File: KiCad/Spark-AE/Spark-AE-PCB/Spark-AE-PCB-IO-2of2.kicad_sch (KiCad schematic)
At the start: 16 parts, among them U6 Connector_Micro_SD_Card_Yamai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, U7 MCP6002-xSN, U8 74LVC1G125

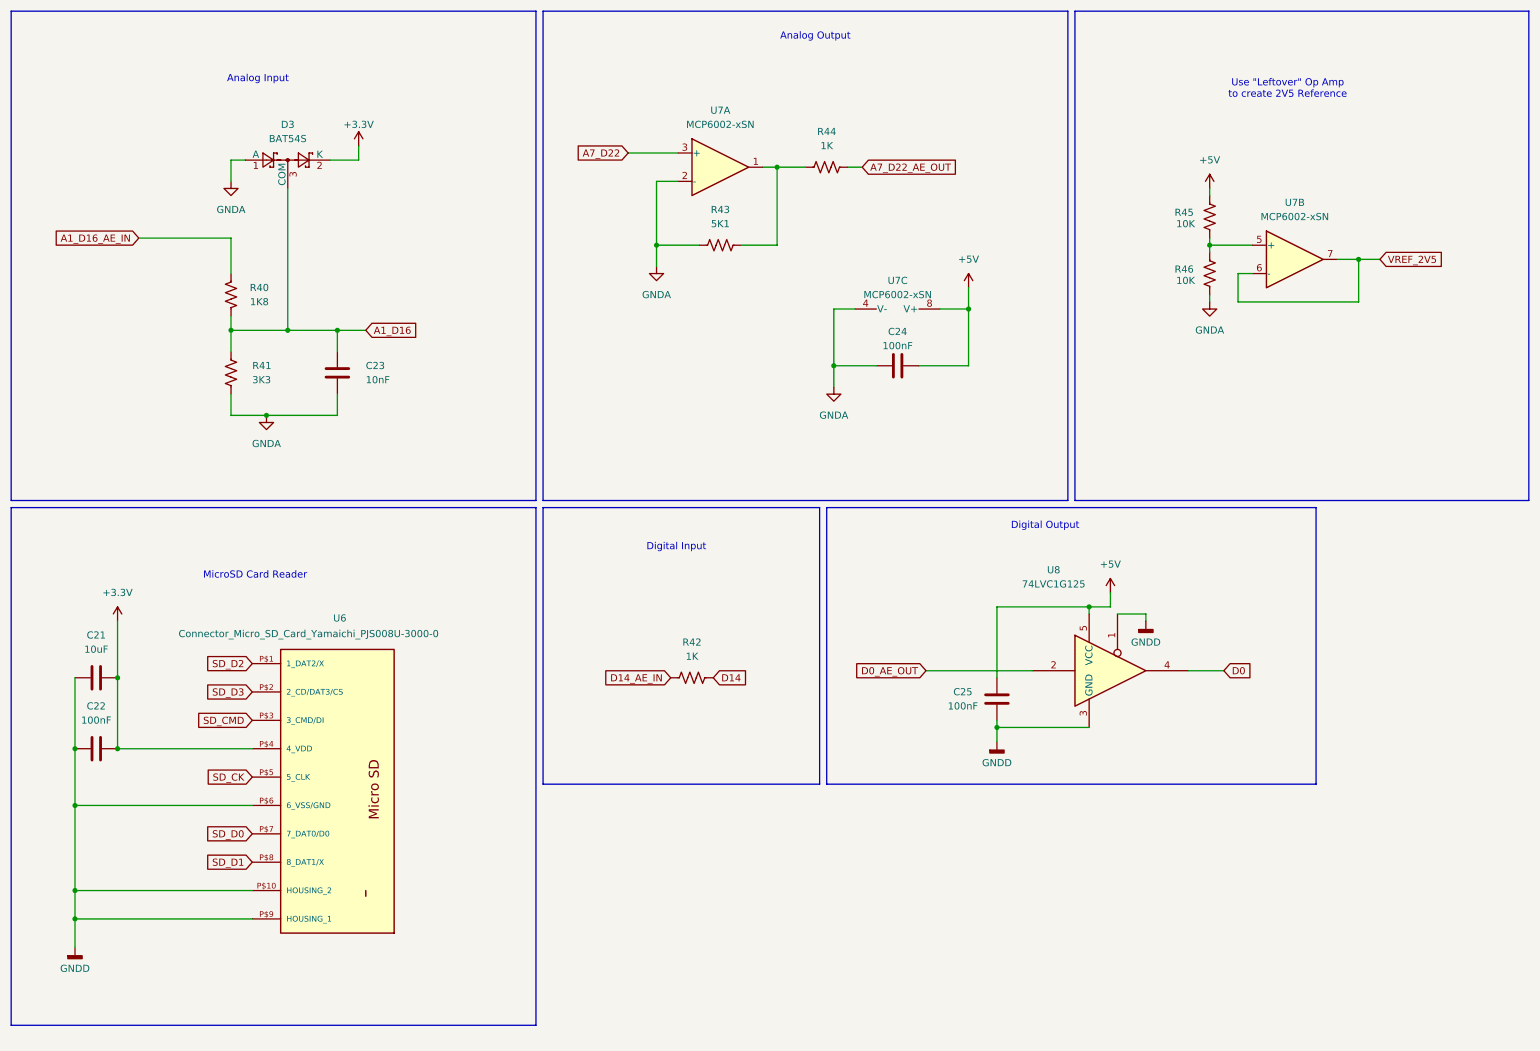
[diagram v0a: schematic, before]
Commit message: assigned footprints & sorted ratsnest
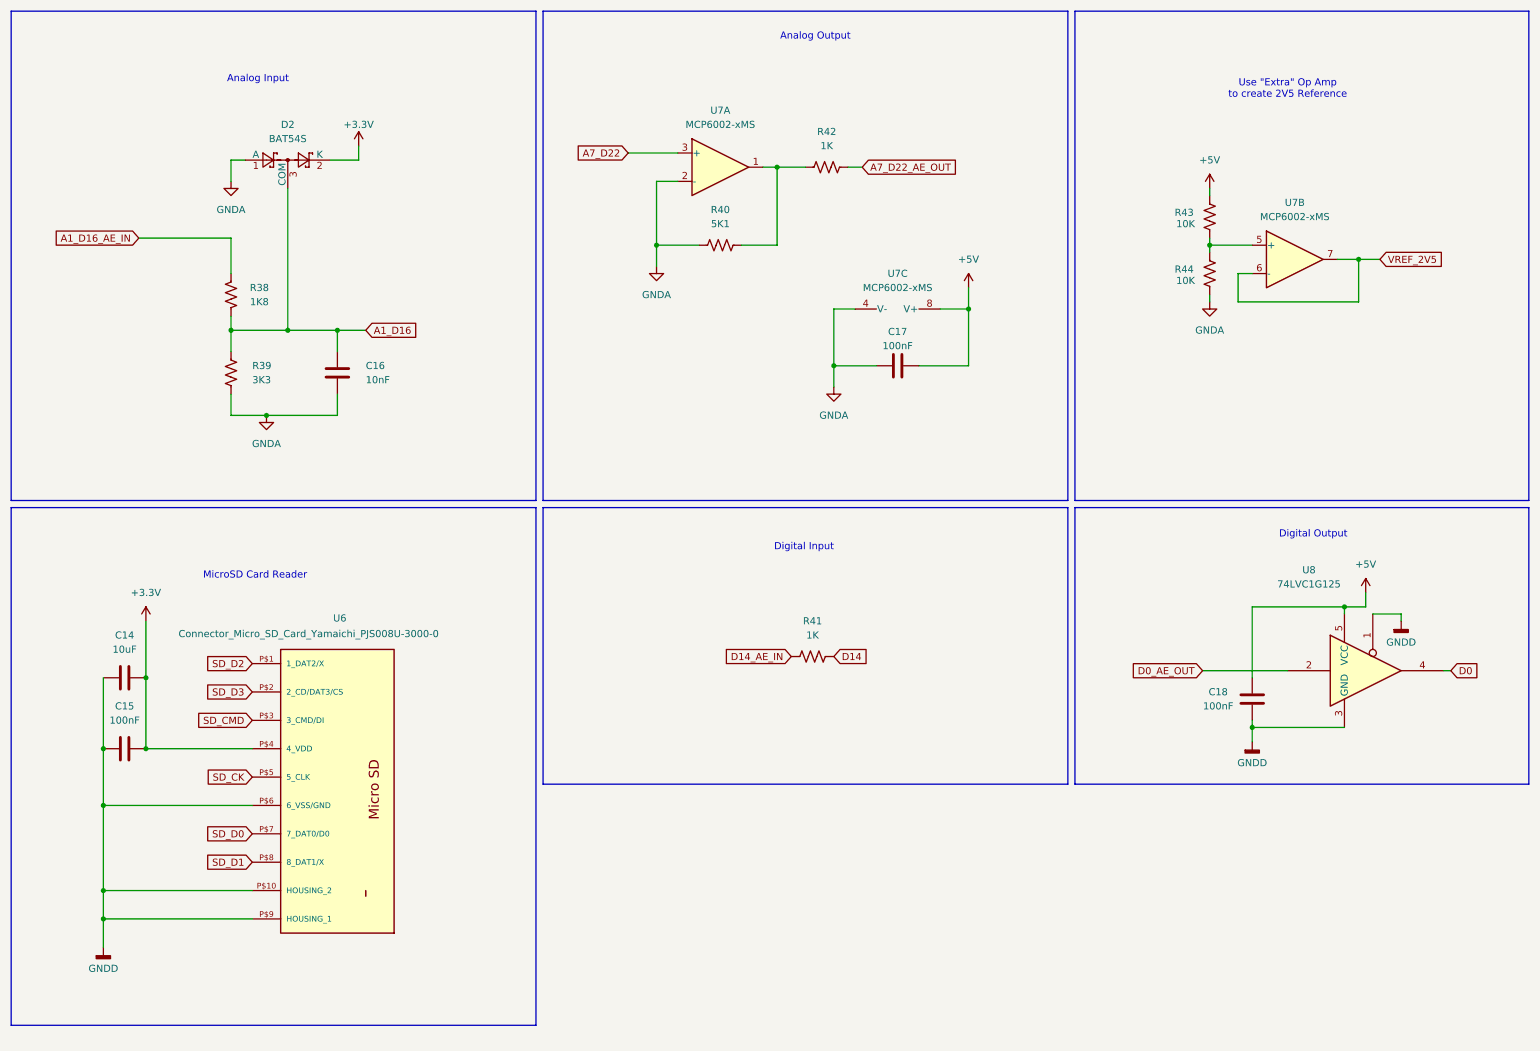
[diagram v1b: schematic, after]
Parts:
- removed U7: MCP6002-xSN, symbol Amplifier_Operational:MCP6002-xSN
- added U7: MCP6002-xMS, clectric-diy:Amplifier_Operational_Microchip_MCP6002T-I_MS, symbol Amplifier_Operational:MCP6002-xMS
- C14: renamed from C21; footprint (none) -> Capacitor_SMD:C_0805_2012Metric
- C15: renamed from C22; footprint (none) -> Capacitor_SMD:C_0603_1608Metric
- C16: renamed from C23; footprint (none) -> Capacitor_SMD:C_0603_1608Metric
- C17: renamed from C24; footprint (none) -> Capacitor_SMD:C_0603_1608Metric
- C18: renamed from C25; footprint (none) -> Capacitor_SMD:C_0603_1608Metric
- R38: renamed from R40; footprint (none) -> Resistor_SMD:R_0603_1608Metric
- R39: renamed from R41; footprint (none) -> Resistor_SMD:R_0603_1608Metric
- R40: renamed from R43; footprint (none) -> Resistor_SMD:R_0603_1608Metric
- R41: renamed from R42; footprint (none) -> Resistor_SMD:R_0603_1608Metric
- R42: renamed from R44; footprint (none) -> Resistor_SMD:R_0603_1608Metric
- R43: renamed from R45; footprint (none) -> Resistor_SMD:R_0603_1608Metric
- R44: renamed from R46; footprint (none) -> Resistor_SMD:R_0603_1608Metric
- U8: footprint (none) -> Package_TO_SOT_SMD:SOT-23-5
- renumbered D3 to D2
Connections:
- net +5V: now also U7.8 (V+)
- net A7_D22: now also U7.3 (+)
- net GNDA: now also U7.2 (-), U7.4 (V-)
- net VREF_2V5: now also U7.6 (-), U7.7
- net at R43.1, R44.2: now also U7.5 (+)
- net at R40.2, R42.1: now also U7.1
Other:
- note added: "Use "Extra" Op Amp to create 2V5 Reference"
- note removed: "Use "Leftover" Op Amp to create 2V5 Reference"
- moved on the sheet: C14, C15, C18, R41, U8

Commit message: schematic 100% complete. pcb layout around 50% complete.
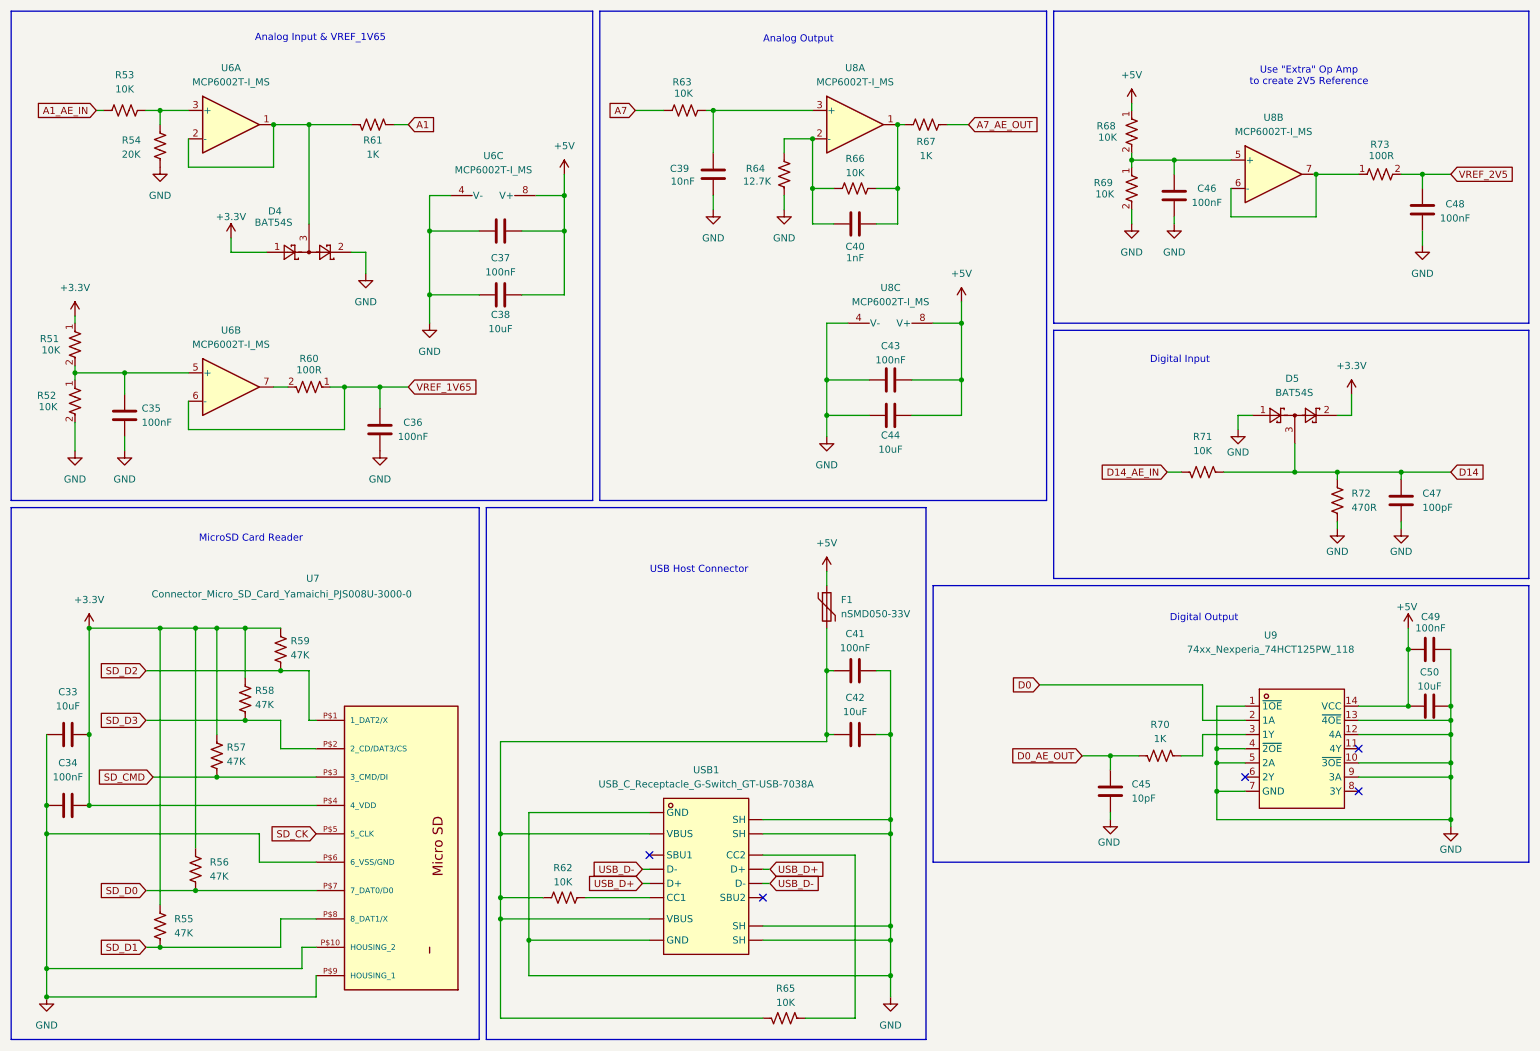
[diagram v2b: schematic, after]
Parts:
- removed C16: 10nF, Capacitor_SMD:C_0603_1608Metric, symbol Device:C
- removed C18: 100nF, Capacitor_SMD:C_0603_1608Metric, symbol Device:C
- removed R39: 3K3, Resistor_SMD:R_0603_1608Metric, symbol Device:R_US
- removed R41: 1K, Resistor_SMD:R_0603_1608Metric, symbol Device:R_US
- removed unit 1 of U7
- removed unit 2 of U7
- removed U8: 74LVC1G125, Package_TO_SOT_SMD:SOT-23-5, symbol 74xGxx:74LVC1G125
- added C35, C36, C37, C41, C46, C48, C49: 100nF, Capacitor_SMD:C_0603_1608Metric, symbol Device:C
- added C38, C42, C44, C50: 10uF, Capacitor_SMD:C_0603_1608Metric, symbol Device:C
- added C39: 10nF, Capacitor_SMD:C_0603_1608Metric, symbol Device:C
- added C40: 1nF, Capacitor_SMD:C_0603_1608Metric, symbol Device:C
- added C45: 10pF, Capacitor_SMD:C_0603_1608Metric, symbol Device:C
- added C47: 100pF, Capacitor_SMD:C_0603_1608Metric, symbol Device:C
- added D5: BAT54S, Package_TO_SOT_SMD:SOT-23, symbol Diode:BAT54S
- added F1: nSMD050-33V, Fuse:Fuse_0603_1608Metric, symbol Device:Polyfuse
- added R51, R52, R53, R62, R63, R65, R71: 10K, Resistor_SMD:R_0603_1608Metric, symbol Device:R_US
- added R54: 20K, Resistor_SMD:R_0603_1608Metric, symbol Device:R_US
- added R55, R56, R57, R58, R59: 47K, Resistor_SMD:R_0603_1608Metric, symbol Device:R_US
- added R60, R73: 100R, Resistor_SMD:R_0603_1608Metric, symbol Device:R_US
- added R64: 12.7K, Resistor_SMD:R_0603_1608Metric, symbol Device:R_US
- added R70: 1K, Resistor_SMD:R_0603_1608Metric, symbol Device:R_US
- added R72: 470R, Resistor_SMD:R_0603_1608Metric, symbol Device:R_US
- added U6: MCP6002T-I_MS, clectric-diy:Amplifier_Operational_Microchip_MCP6002T-I_MS, symbol clectric-diy:Amplifier_Operational_Microchip_MCP6002-xSN
- added unit 2 of U8
- added unit 1 of U8
- added U9: 74xx_Nexperia_74HCT125PW_118, clectric-diy:74xx_Nexperia_74HCT125PW_118, symbol clectric-diy:74xx_Nexperia_74HCT125PW_118
- added USB1: USB_C_Receptacle_G-Switch_GT-USB-7038A, clectric-diy:USB_C_Receptacle_G-Switch_GT-USB-7038A, symbol clectric-diy:USB_C_Receptacle_G-Switch_GT-USB-7038A
- C33: renamed from C14; footprint Capacitor_SMD:C_0805_2012Metric -> Capacitor_SMD:C_0603_1608Metric
- R61: renamed from R38; value 1K8 -> 1K
- R66: renamed from R40; value 5K1 -> 10K
- U8: renamed from U7; value MCP6002-xMS -> MCP6002T-I_MS
- renumbered C15 to C34, C17 to C43, D2 to D4, R42 to R67, R43 to R68, R44 to R69, U6 to U7
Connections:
- net A1_D16_AE_IN is gone; now on an unnamed net: R61.2
- net GNDD is gone; now on net GND: C33.2, C34.2, U7.P$10 (HOUSING_2), U7.P$6 (6_VSS/GND), U7.P$9 (HOUSING_1)
- net +3.3V: now also D4.1 (A), D5.2 (K), R51.1, R55.1, R56.1, R57.1, R58.1, R59.1; no longer D4.2 (K)
- net +5V: now also R68.1, C37.2, C38.2, C44.2, C49.1, C50.2, F1.1, U6.8 (V+), U9.14 (VCC); no longer R68.2
- net D0: now also U9.2 (1A)
- net D0_AE_OUT: now also C45.1, R70.1
- net D14: now also C47.1, D5.3 (COM), R71.2, R72.1
- net D14_AE_IN: now also R71.1
- net SD_CMD: now also R57.2
- net SD_D0: now also R56.2
- net SD_D1: now also R55.2
- net SD_D2: now also R59.2
- net SD_D3: now also R58.2
- net VREF_2V5: now also C48.2, R73.2
- net GND: now reaches R69.2
- net GND: now also C43.1, D4.2 (K), U8.4 (V-), C35.2, C36.2, C37.1, C38.1, C39.2, C41.1, C42.1, C44.1, C45.2, C46.2, C47.2, C48.1, C49.2, C50.1, D5.1 (A), R52.2, R54.2, R64.1, R72.2, U6.4 (V-), U9.1 (~{1OE}), U9.10 (~{3OE}), U9.12 (4A), U9.13 (~{4OE}), U9.4 (~{2OE}), U9.5 (2A), U9.7 (GND), U9.9 (3A), USB1.17 (SH), USB1.18 (SH), USB1.19 (SH), USB1.20 (SH), USB1.A12B1 (GND), USB1.A1B12 (GND); no longer R68.1
- net at R66.2, R67.1: now also C40.1, U8.1
- net A1_D16: no longer names the net of D4.3 (COM)
- net A1_D16: now also U6.1, U6.2 (-); no longer R61.1
- net A7_D22_AE_OUT renamed A7_AE_OUT
- removed net GNDA: C43.1, D4.1 (A), R66.1, R69.1, U8.4 (V-)
- new net: R53.2, R54.1, U6.3 (+)
- new net: C46.1, R68.2, R69.1, U8.5 (+)
- new net: C41.2, C42.2, F1.2, R62.1, R65.2, USB1.A4B9 (VBUS), USB1.A9B4 (VBUS)
- new net: R62.2, USB1.A5 (CC1)
- new net: C39.1, R63.2, U8.3 (+)
- new net: C40.2, R64.2, R66.1, U8.2 (-)
- new net: R73.1, U8.6 (-), U8.7
- new net: C35.1, R51.2, R52.1, U6.5 (+)
- new net: R65.1, USB1.B5 (CC2)
- new net: R60.2, U6.7
- new net: R70.2, U9.3 (1Y)
- new net A1: R61.1
- new net A1_AE_IN: R53.1
- new net A7: R63.1
- new net USB_D+: USB1.A6 (D+), USB1.B6 (D+)
- new net USB_D-: USB1.A7 (D-), USB1.B7 (D-)
- new net VREF_1V65: C36.1, R60.1, U6.6 (-)
- no-connect marks 0 -> 5
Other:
- note added: "Analog Input & VREF_1V65"
- note added: "USB Host Connector"
- note removed: "Analog Input"
- moved on the sheet: C33, C34, C43, R61, R66, R67, U7, U8C

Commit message: continuing to plug away at pcb layout
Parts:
- R51, R52, R68, R69: value 10K -> 100K
- renumbered C33 to C31, C34 to C32, C35 to C33, C36 to C34, C37 to C35, C38 to C36, C39 to C37, C40 to C38, C41 to C39, C42 to C40, C43 to C41, C44 to C42, C45 to C43, C46 to C44, C47 to C45, C48 to C46, C49 to C47, C50 to C48
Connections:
- net A1: now also R61.2; no longer R61.1
- net VREF_2V5: now also U8.6 (-)
- net at D4.3 (COM), U6.1, U6.2 (-): now also R61.1; no longer R61.2
- net at R73.1, U8.7: no longer U8.6 (-)
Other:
- moved on the sheet: C33, C34, R51, R52, R60, R61, R73, U6B

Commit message: I accdently upgraded to KiCad 10 via a `brew upgrade`. I committing before launching it just in case.
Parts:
- removed C39: 100nF, Capacitor_SMD:C_0603_1608Metric, symbol Device:C
- removed C40: 10uF, Capacitor_SMD:C_0603_1608Metric, symbol Device:C
- removed F1: nSMD050-33V, Fuse:Fuse_0603_1608Metric, symbol Device:Polyfuse
- removed U9: 74xx_Nexperia_74HCT125PW_118, clectric-diy:74xx_Nexperia_74HCT125PW_118, symbol clectric-diy:74xx_Nexperia_74HCT125PW_118
- removed USB1: USB_C_Receptacle_G-Switch_GT-USB-7038A, clectric-diy:USB_C_Receptacle_G-Switch_GT-USB-7038A, symbol clectric-diy:USB_C_Receptacle_G-Switch_GT-USB-7038A
- added C55: 100nF, Capacitor_SMD:C_0603_1608Metric, symbol Device:C
- added C56: 10uF, Capacitor_SMD:C_0603_1608Metric, symbol Device:C
- added F2: nSMD050-33V, Fuse:Fuse_0603_1608Metric, symbol Device:Polyfuse
- added U9: 74xGxx_MDD_74AHCT1G125GV, clectric-diy:74xGxx_MDD_74AHCT1G125GV, symbol clectric-diy:74xGxx_MDD_74AHCT1G125GV
- added USB1: USB_C_Receptacle_H8.8mm_Jing_918-648K2027E30002, clectric-diy:USB_C_Receptacle_H8.8mm_Jing_918-648K2027E30002, symbol clectric-diy:USB_C_Receptacle_H8.8mm_Jing_918-648K2027E30002
- R62, R65: value 10K -> 56K
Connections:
- net +5V: now also F2.1, U9.5 (VCC)
- net D0: now also U9.2 (A)
- net GND: now also C55.2, C56.2, U9.1 (~{OE}), U9.3 (GND), USB1.2, USB1.3, USB1.4, USB1.5, USB1.A1 (GND), USB1.A12 (GND), USB1.B1 (GND), USB1.B12 (GND)
- net USB_D+: now also USB1.A6 (D+), USB1.B6 (D+)
- net USB_D-: now also USB1.A7 (D-), USB1.B7 (D-)
- net at R62.1: now also R65.1, C55.1, C56.1, F2.2, USB1.A4 (VBUS), USB1.A9 (VBUS), USB1.B4 (VBUS), USB1.B9 (VBUS); no longer R65.2
- net at R62.2: now also USB1.A5 (CC1)
- net at R70.2: now also U9.4 (Y)
- new net: R65.2, USB1.B5 (CC2)
- no-connect marks 5 -> 2
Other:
- moved on the sheet: C43, C47, C48, R62, R65, R70

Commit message: pcb layout complete. ready for final pre-fab confirmation.
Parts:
- removed C31: 10uF, Capacitor_SMD:C_0603_1608Metric, symbol Device:C
- removed C32: 100nF, Capacitor_SMD:C_0603_1608Metric, symbol Device:C
- removed R55, R56, R57, R58, R59: 47K, Resistor_SMD:R_0603_1608Metric, symbol Device:R_US
- removed U7: Connector_Micro_SD_Card_Yamaichi_PJS008U-3000-0, clectric-diy:PJS008U-3000-0, symbol clectric-diy:Connector_Micro_SD_Card_Yamaichi_PJS008U-3000-0
- added J7: SD_CONN, Connector_PinSocket_2.54mm:PinSocket_2x04_P2.54mm_Vertical, symbol Connector_Generic:Conn_02x04_Odd_Even
- renumbered C55 to C39, C56 to C40, C44 to C43, C47 to C44, C48 to C45, C45 to C46, C43 to C47, C46 to C48, F2 to F1, R51 to R53, R52 to R54, R53 to R55, R54 to R56, R60 to R62, R61 to R63, R62 to R64, R63 to R65, R64 to R66, R65 to R67, R66 to R68, R67 to R69, R68 to R70, R69 to R71, R71 to R72, R72 to R73, R73 to R74, R70 to R75
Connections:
- net +3.3V: now also J7.6 (Pin_6)
- net GND: now also J7.8 (Pin_8)
- net SD_CK: now also J7.4 (Pin_4)
- net SD_CMD: now also J7.2 (Pin_2)
- net SD_D0: now also J7.1 (Pin_1)
- net SD_D1: now also J7.3 (Pin_3)
- net SD_D2: now also J7.5 (Pin_5)
- net SD_D3: now also J7.7 (Pin_7)
- net VREF_1V65: now also R62.2; no longer R62.1
- net at U6.7: now also R62.1; no longer R62.2
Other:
- note added: "MicroSD Card Reader Connector (Reader on Panel)"
- note removed: "MicroSD Card Reader"
- moved on the sheet: R62, R66
